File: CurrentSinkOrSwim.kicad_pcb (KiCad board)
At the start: 2 copper layers, 41.7 x 47.8 mm, 23 parts, among them P1 CONN_01X01, P101 CONN_01X02, P102 CONN_01X03, P103 CONN_01X02, Q401 BUK9575, U201 LMV358, U301 LM2931D-R

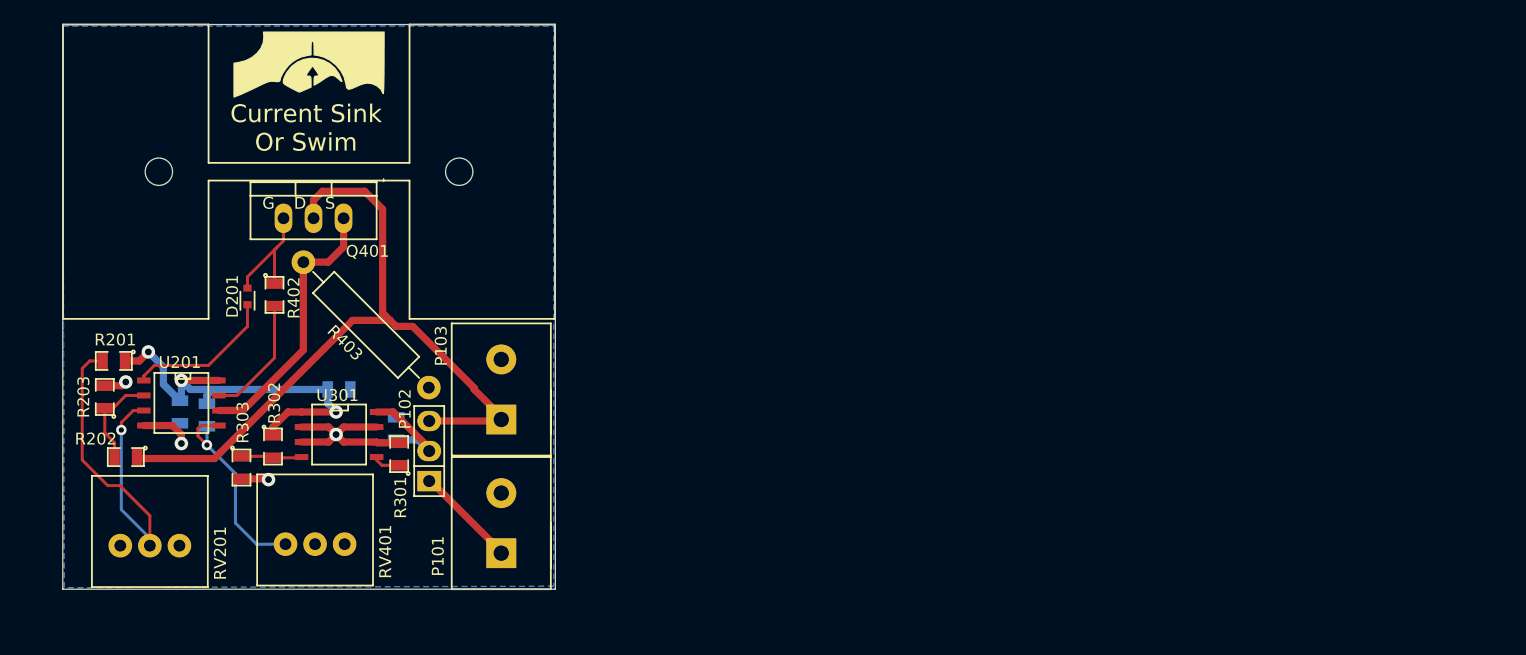
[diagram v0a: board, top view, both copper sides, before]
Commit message: added measure pins and ripup layout
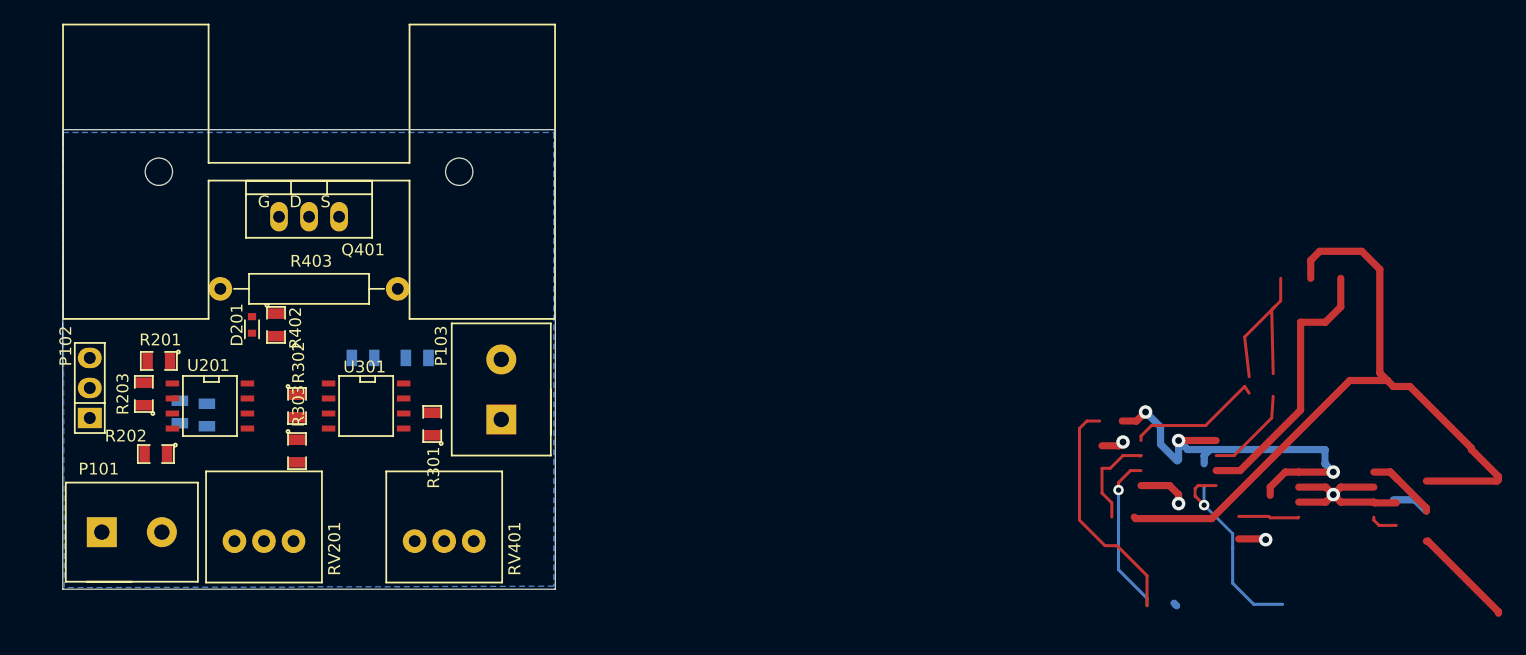
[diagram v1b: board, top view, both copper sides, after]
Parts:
- removed G***: LOGO, Current:CSOS
- moved P101 31.3 mm to (112.0, 78.7), turned to 0 degrees
- moved P102 29.2 mm to (108.5, 66.5)
- moved RV401 10.9 mm to (138.4, 79.5)
- moved RV201 9.66 mm to (123.2, 79.5)
- moved C301 6.23 mm to (136.1, 64.0), turned to 180 degrees
- moved R403 5.71 mm to (127.0, 58.2), turned to 180 degrees
- moved R303 4.90 mm to (126.0, 71.9)
- moved R302 3.99 mm to (126.0, 68.1)
- moved R201 3.81 mm to (114.3, 64.3)
- moved R301 3.78 mm to (137.4, 69.6)
- moved C302 3.35 mm to (131.6, 64.0)
- moved U301 3.32 mm to (131.8, 68.1)
- moved R203 3.31 mm to (113.0, 67.1)
- moved R202 2.55 mm to (114.0, 72.1)
- moved R402 2.54 mm to (124.2, 61.2)
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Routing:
- net (no net): track 0.00 -> 267.2 mm, vias 0 -> 9
- net /Current Control/Current_Sink+: track 63.5 -> 0.00 mm
- net 2.7V: track 35.3 -> 0.00 mm, vias 3 -> 0
- net Net-(R201-Pad2): track 33.7 -> 0.00 mm, vias 1 -> 0
- net GND: track 24.5 -> 0.00 mm, vias 4 -> 0
- net Net-(Q401-PadS): track 23.0 -> 0.00 mm
- net Net-(R401-Pad2): track 17.9 -> 0.00 mm, vias 1 -> 0
- net Net-(D201-Pad2): track 12.7 -> 0.00 mm
- net Net-(R402-Pad2): track 10.4 -> 0.00 mm
- net /Current Control/FET_Gate: track 10.4 -> 0.00 mm
- net /Power Regulation/Vin: track 10.0 -> 0.00 mm
- net Net-(P101-Pad1): track 8.70 -> 0.00 mm
- net Net-(R202-Pad2): track 8.31 -> 0.00 mm
- net Net-(R302-Pad2): track 5.16 -> 0.00 mm
- net Net-(R301-Pad1): track 2.34 -> 0.00 mm
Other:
- board size 41.7 x 47.8 mm -> 41.7 x 38.9 mm
- board text removed: "Current Sink Or Swim"

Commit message: Changed footprints, changed layout
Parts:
- added P2: V, Pin_Headers:Pin_Header_Straight_1x01, F.Cu at (109.0, 75.5)
- added P3: A, Pin_Headers:Pin_Header_Straight_1x01, F.Cu at (114.2, 81.0)
- added P4: Gnd, Pin_Headers:Pin_Header_Straight_1x01, F.Cu at (109.5, 80.2)
- P101: value CONN_01X02 -> ext pwr; footprint Current:Terminal_Block_200_mil -> Current:Pads-01x02
- P102: value CONN_01X03 -> pwr select
- P103: value CONN_01X02 -> Input; footprint Current:Terminal_Block_200_mil -> Current:TB-01x02
- Q401: footprint Transistors_TO-220:TO-220_FET-GDS_Vertical -> Current:current-TO-220_FET-GDS_Vertical
- R403: footprint Resistors_ThroughHole:Resistor_Horizontal_RM15mm -> Current:1W-Resistor
- moved P102 36.2 mm to (143.0, 77.2)
- moved P101 23.8 mm to (135.8, 80.5)
- moved RV201 18.4 mm to (109.0, 67.8), turned to 270 degrees
- moved RV401 16.0 mm to (122.5, 80.8)
- moved R203 10.9 mm to (120.8, 74.8), turned to 180 degrees
- moved R202 10.5 mm to (124.2, 74.8)
- moved R301 6.43 mm to (133.2, 74.5), turned to 0 degrees
- moved C201 5.06 mm to (121.0, 69.8), turned to 0 degrees
- moved C302 4.81 mm to (130.8, 68.8), turned to 90 degrees
- moved C301 4.76 mm to (135.8, 68.8), turned to 90 degrees
- moved R201 3.50 mm to (114.0, 67.8)
- moved R402 3.22 mm to (121.2, 62.5)
- moved R401 2.85 mm to (121.0, 67.8), turned to 0 degrees
- moved U201 2.48 mm to (121.0, 68.8), turned to 0 degrees
- moved U301 1.58 mm to (133.2, 68.8), turned to 180 degrees
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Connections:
- P101 pad 1: Net-(P101-Pad1) -> GND
- P101 pad 2: GND -> Net-(P101-Pad2)
- P102 pad 1: Net-(P101-Pad1) -> Net-(P101-Pad2)
- P103 pad 1: /Current Control/Current_Sink+ -> GND
- P103 pad 2: GND -> /Current Control/Current_Sink+
- R401 pad 2: Net-(R401-Pad2) -> Net-(P3-Pad1)
- RV201 pad 1: Net-(RV201-Pad1) -> (no net)
- RV401 pad 1: Net-(R401-Pad2) -> (no net)
- RV401 pad 2: GND -> Net-(P3-Pad1)
- RV401 pad 3: Net-(RV401-Pad3) -> GND
- U201 pad 5: Net-(R401-Pad2) -> Net-(P3-Pad1)
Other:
- board text added: "+"
- board text added: "-"
- board text added: "ext"
- board text added: "in"

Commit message: Routing done - Final
Just add artwork
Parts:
- C201, C301, C302, R401: moved to F.Cu
- P101: footprint Current:Pads-01x02 -> Pads-01x02
- P102: value pwr select -> pwr sel
- R403: footprint Current:1W-Resistor -> 1W-Resistor
- moved R201 10.4 mm to (124.0, 65.0), turned to 270 degrees
- moved D201 6.98 mm to (116.4, 63.6)
- moved C302 6.73 mm to (136.2, 64.8), turned to 270 degrees
- moved C201 6.60 mm to (121.8, 63.2), turned to 90 degrees
- moved R401 5.71 mm to (126.0, 65.0), turned to 270 degrees
- moved R301 4.29 mm to (129.4, 72.6), turned to 180 degrees
- moved R302 2.37 mm to (128.0, 65.0)
- moved U201 2.32 mm to (118.8, 68.0), turned to 270 degrees
- moved U301 1.87 mm to (132.2, 67.2)
- moved R402 1.79 mm to (119.6, 63.2)
- moved R303 1.77 mm to (128.0, 69.4)
- moved R202 1.32 mm to (123.6, 73.6), turned to 90 degrees
- moved R203 1.23 mm to (121.2, 73.6), turned to 270 degrees
- moved C301 1.14 mm to (136.2, 69.8)
- moved P101 0.90 mm to (135.0, 80.0)
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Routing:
- net (no net): track 267.2 -> 0.00 mm, vias 9 -> 0
- net /Current Control/Current_Sink+: track 0.00 -> 57.6 mm
- net GND: track 0.00 -> 35.1 mm, vias 0 -> 5
- net Net-(P3-Pad1): track 0.00 -> 29.6 mm, vias 0 -> 2
- net Net-(P2-Pad1): track 0.00 -> 28.8 mm, vias 0 -> 2
- net Net-(Q401-PadS): track 0.00 -> 26.5 mm, vias 0 -> 2
- net 2.7V: track 0.00 -> 19.8 mm
- net /Current Control/FET_Gate: track 0.00 -> 16.2 mm
- net /Power Regulation/Vin: track 0.00 -> 12.7 mm, vias 0 -> 1
- net Net-(R202-Pad2): track 0.00 -> 11.5 mm
- net Net-(R302-Pad2): track 0.00 -> 7.21 mm
- net Net-(P101-Pad2): track 0.00 -> 6.05 mm
- net Net-(R402-Pad2): track 0.00 -> 5.02 mm
- net Net-(R301-Pad1): track 0.00 -> 2.25 mm
- net Net-(D201-Pad2): track 0.00 -> 2.12 mm
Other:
- board size 41.7 x 38.9 mm -> 41 x 38 mm
- board text added: "Amp"
- board text added: "Volt"
- board text added: "int"
- board text removed: "in"

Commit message: Final done - Uploaded to OSHPark
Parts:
- added G***: LOGO, -PB_Logo:pb-nietje-10mm-mask, B.Cu at (127.0, 65.0)
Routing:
- net GND: track 35.1 -> 38.2 mm
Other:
- board text added: "Current Sink (or Swim)"
